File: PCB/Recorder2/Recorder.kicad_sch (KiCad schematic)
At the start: 57 parts, among them J1 Reset, J2 JST-PH-SM4-TB, J3 TC2030-USB-NL-DS, J4 TF_PUSH, J5 USB-C-Socket-H, Q1 CJ2301, SW1 SW_Push_DPDT, U1 ESP32-S3-MINI-1-N4R2, U3 TP4054, U4 ME6211C33M5G-N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

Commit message: Tracked for order
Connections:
- net ADC: now also U1.14 (GPIO10)
- net ADCL: now also U1.15 (GPIO11)
- net BLINK: now also U1.29 (GPIO34); no longer U1.35 (GPIO39)
- net BTN: now also U1.7 (GPIO3); no longer U1.5 (GPIO1)
- net CHARGING: now also U1.5 (GPIO1); no longer U1.15 (GPIO11)
- net LEDMIC: now also U1.13 (GPIO9); no longer U1.12 (GPIO8)
- net at U1.30 (GPIO48): now also R1.1
- net at U1.37 (GPIO41): no longer R1.1
- net VIN: no longer names the net of D3.1 (K), Q1.2 (S), U4.1 (IN), U4.3 (EN)
- no-connect marks 22 -> 20
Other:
- moved on the sheet: R1
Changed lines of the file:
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@@
 	)
 	(junction
-		(at 196.85 133.985)
-		(diameter 0)
-		(color 0 0 0 0)
-	)
-	(junction
 		(at 247.65 22.86)
 		(diameter 0)
@@
 	)
 	(no_connect
-		(at 66.04 88.9)
+		(at 66.04 86.36)
 	)
 	(no_connect
@@
 	)
 	(no_connect
-		(at 66.04 101.6)
+		(at 66.04 81.28)
 	)
 	(no_connect
@@
 	)
 	(no_connect
-		(at 35.56 58.42)
-	)
-	(no_connect
 		(at 66.04 71.12)
 	)
@@
 	)
 	(no_connect
-		(at 35.56 73.66)
-	)
-	(no_connect
 		(at 66.04 93.98)
 	)
 	(no_connect
-		(at 35.56 55.88)
+		(at 35.56 58.42)
 	)
 	(no_connect
@@
 	)
 	(no_connect
-		(at 66.04 68.58)
+		(at 66.04 88.9)
 	)
 	(no_connect
@@
 	)
 	(no_connect
-		(at 35.56 71.12)
+		(at 35.56 68.58)
 	)
 	(wire
@@
 	(wire
 		(pts
+			(xy 73.66 90.805) (xy 70.485 90.805)
+		)
+		(stroke
+			(width 0)
+			(type default)
+		)
+	)
+	(wire
+		(pts
 			(xy 273.05 121.285) (xy 273.05 122.555)
 		)
@@
 	(wire
 		(pts
+			(xy 70.485 90.805) (xy 70.485 101.6)
+		)
+		(stroke
+			(width 0)
+			(type default)
+		)
+	)
+	(wire
+		(pts
 			(xy 137.16 70.485) (xy 137.16 74.295)
 		)
@@
 	(wire
 		(pts
+			(xy 70.485 101.6) (xy 66.04 101.6)
+		)
+		(stroke
+			(width 0)
+			(type default)
+		)
+	)
+	(wire
+		(pts
 			(xy 121.92 62.865) (xy 125.73 62.865)
 		)
@@
 	(wire
 		(pts
-			(xy 196.85 133.985) (xy 196.85 139.7)
-		)
-		(stroke
-			(width 0)
-			(type default)
-		)
-	)
-	(wire
-		(pts
 			(xy 110.49 76.835) (xy 133.35 76.835)
 		)
@@
 	(global_label "BTN"
 		(shape input)
-		(at 35.56 50.8 180)
+		(at 35.56 55.88 180)
 		(fields_autoplaced yes)
 		(effects
@@
 		)
 		(property "Intersheetrefs" "${INTERSHEET_REFS}"
-			(at 29.6609 50.8 0)
+			(at 29.6609 55.88 0)
 			(effects
 				(font
@@
 	(global_label "CHARGING"
 		(shape input)
-		(at 35.56 76.2 180)
-		(fields_autoplaced yes)
-		(effects
-			(font
-				(size 1.27 1.27)
-			)
-			(justify right)
-		)
-		(property "Intersheetrefs" "${INTERSHEET_REFS}"
-			(at 23.7946 76.2 0)
-			(effects
-				(font
-					(size 1.27 1.27)
-				)
-				(justify right)
-				(hide yes)
-			)
-		)
-	)
-	(global_label "VIN"
-		(shape output)
-		(at 196.85 139.7 270)
+		(at 35.56 50.8 180)
 		(fields_autoplaced yes)
 		(effects
@@
 		)
 		(property "Intersheetrefs" "${INTERSHEET_REFS}"
-			(at 196.85 145.0549 90)
+			(at 23.7946 50.8 0)
 			(effects
 				(font
@@
 		)
 	)
+	(global_label "ADC"
+		(shape input)
+		(at 35.56 73.66 180)
+		(effects
+			(font
+				(size 1.27 1.27)
+			)
+			(justify right)
+		)
+		(property "Intersheetrefs" "${INTERSHEET_REFS}"
+			(at 35.56 73.66 0)
+			(effects
+				(font
+					(size 1.27 1.27)
+				)
+				(hide yes)
+			)
+		)
+	)
 	(global_label "VBUS"
 		(shape output)
@@
 	(global_label "VBUS"
 		(shape input)
-		(at 73.66 86.36 0)
+		(at 81.28 90.805 0)
 		(fields_autoplaced yes)
 		(effects
@@
 		)
 		(property "Intersheetrefs" "${INTERSHEET_REFS}"
-			(at 80.8896 86.36 0)
+			(at 88.5096 90.805 0)
 			(effects
 				(font
@@
 	(global_label "LEDMIC"
 		(shape output)
-		(at 35.56 68.58 180)
+		(at 35.56 71.12 180)
 		(fields_autoplaced yes)
 		(effects
@@
 		)
 		(property "Intersheetrefs" "${INTERSHEET_REFS}"
-			(at 26.4557 68.58 0)
+			(at 26.4557 71.12 0)
 			(effects
 				(font
@@
 	(global_label "BLINK"
 		(shape output)
-		(at 66.04 81.28 0)
+		(at 66.04 68.58 0)
 		(fields_autoplaced yes)
 		(effects
@@
 		)
 		(property "Intersheetrefs" "${INTERSHEET_REFS}"
-			(at 73.8744 81.28 0)
+			(at 73.8744 68.58 0)
 			(effects
 				(font
@@
 		)
 	)
+	(global_label "ADCL"
+		(shape bidirectional)
+		(at 35.56 76.2 180)
+		(effects
+			(font
+				(size 1.27 1.27)
+			)
+			(justify right)
+		)
+		(property "Intersheetrefs" "${INTERSHEET_REFS}"
+			(at 35.56 76.2 0)
+			(effects
+				(font
+					(size 1.27 1.27)
+				)
+				(hide yes)
+			)
+		)
+	)
 	(global_label "SDDAT2"
 		(shape bidirectional)
@@
 	(symbol
 		(lib_id "Device:R")
-		(at 69.85 86.36 90)
+		(at 77.47 90.805 90)
 		(unit 1)
 		(exclude_from_sim no)
@@
 		(dnp no)
 		(property "Reference" "R1"
-			(at 69.85 84.455 90)
+			(at 77.47 88.9 90)
 			(effects
 				(font
@@
 		)
 		(property "Value" "10K"
-			(at 69.85 86.36 90)
+			(at 77.47 90.805 90)
 			(effects
 				(font
@@
 		)
 		(property "Footprint" "RevK:R_0201"
-			(at 69.85 88.138 90)
+			(at 77.47 92.583 90)
 			(effects
 				(font
@@
 		)
 		(property "Datasheet" "~"
-			(at 69.85 86.36 0)
+			(at 77.47 90.805 0)
 			(effects
 				(font
@@
 		)
 		(property "Description" "Resistor"
-			(at 69.85 86.36 0)
+			(at 77.47 90.805 0)
 			(effects
 				(font

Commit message: Re render
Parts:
- C10, C11: footprint RevK:C_0402 -> RevK:C_0201
- J2: Rotation Offset (none) -> 180
- R1, R10, R2, R3, R4, R5, R6, R7, R9: MPN (none) -> C106225
- R11: footprint RevK:R_0402 -> RevK:R_0201; MPN (none) -> C106225
- R12, R13: MPN (none) -> C274341
- R14, R15, R16: footprint RevK:R_0402 -> RevK:R_0201; MPN C5139597 -> C717003
- R8: value 10K -> 5K1; footprint RevK:R_0402 -> RevK:R_0201; MPN (none) -> C274341
- U4: Rotation Offset (none) -> 90
- U5: value L -> ICS-43434
- U6: value R -> ICS-43434
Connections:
- net ADC: now also U1.15 (GPIO11); no longer U1.14 (GPIO10)
- net GND: now also R16.2
- removed net ADCL: R16.2, U1.15 (GPIO11)
- no-connect marks 20 -> 21
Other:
- note added: "5k1 is approx 200mA charge"
- note added: "CHRG Normal: on Full: off Reverse: off No battery: Twinkle"
- note added: "L"
- note added: "R"

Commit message: Layout tweaks
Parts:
- U2: value ~ -> TPS22916CNYFPR
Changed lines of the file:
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@@
 			)
 		)
-		(property "Value" "~"
+		(property "Value" "TPS22916CNYFPR"
 			(at 67.818 143.2949 0)
 			(effects

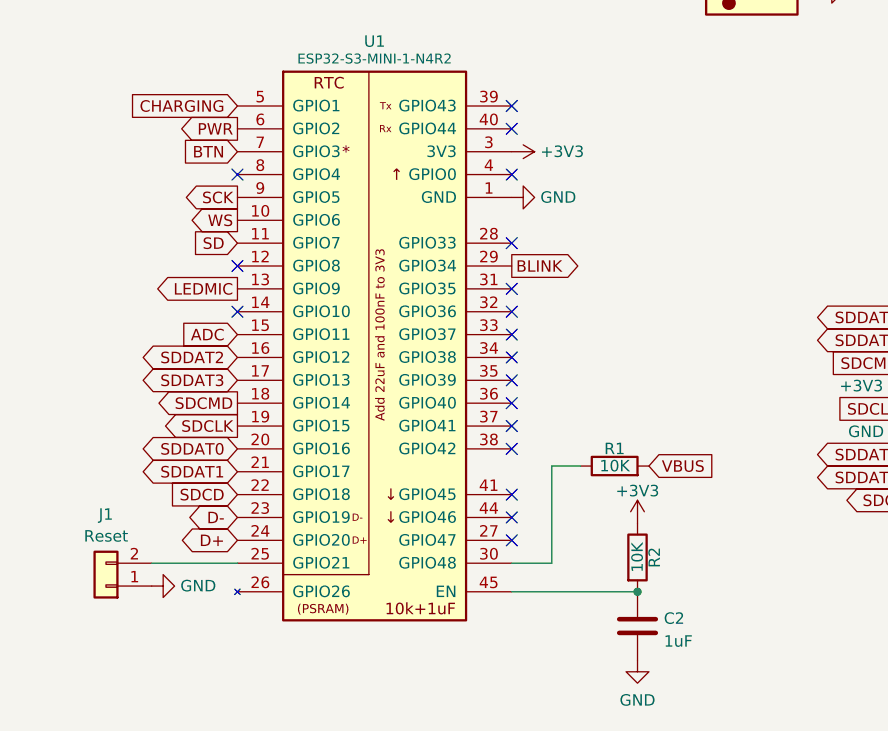
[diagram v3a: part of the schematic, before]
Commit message: Moved GPIOs around a bit
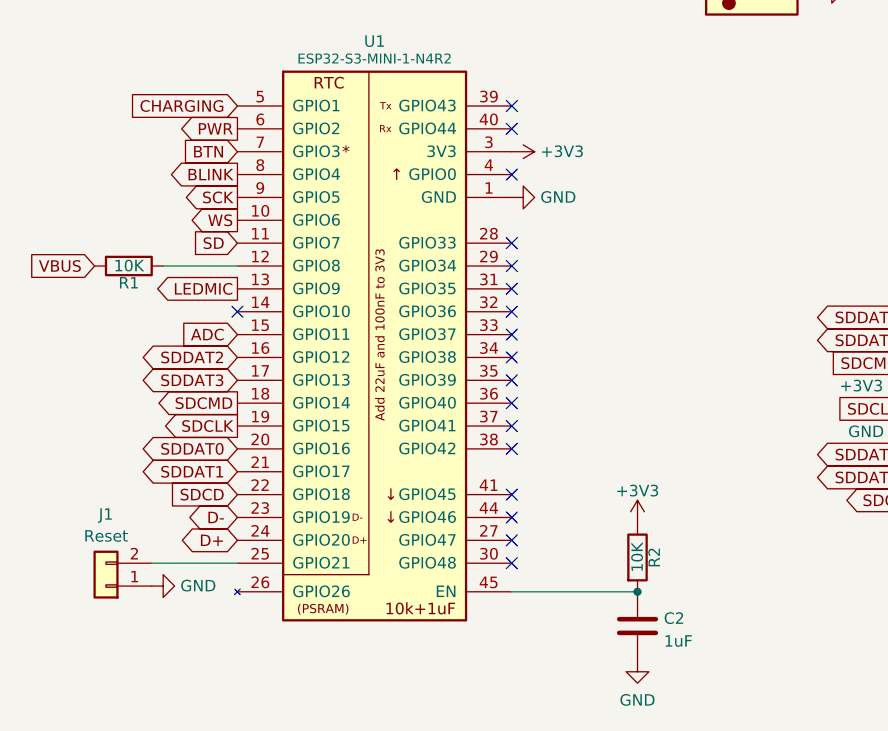
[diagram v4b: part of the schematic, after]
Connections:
- net BLINK: now also U1.8 (GPIO4); no longer U1.29 (GPIO34)
- net at U1.12 (GPIO8): now also R1.1
- net at U1.30 (GPIO48): no longer R1.1
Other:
- moved on the sheet: R1
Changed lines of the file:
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@@
 	)
 	(no_connect
-		(at 35.56 58.42)
+		(at 66.04 68.58)
 	)
 	(no_connect
@@
 	)
 	(no_connect
-		(at 35.56 68.58)
+		(at 66.04 101.6)
 	)
 	(wire
@@
 	(wire
 		(pts
-			(xy 73.66 90.805) (xy 70.485 90.805)
-		)
-		(stroke
-			(width 0)
-			(type default)
-		)
-	)
-	(wire
-		(pts
 			(xy 273.05 121.285) (xy 273.05 122.555)
 		)
@@
 	(wire
 		(pts
-			(xy 70.485 90.805) (xy 70.485 101.6)
-		)
-		(stroke
-			(width 0)
-			(type default)
-		)
-	)
-	(wire
-		(pts
 			(xy 137.16 70.485) (xy 137.16 74.295)
 		)
@@
 	(wire
 		(pts
-			(xy 239.395 52.705) (xy 239.395 57.15)
+			(xy 27.305 68.58) (xy 35.56 68.58)
 		)
 		(stroke
@@
 	(wire
 		(pts
-			(xy 57.785 156.845) (xy 57.785 164.465)
+			(xy 239.395 52.705) (xy 239.395 57.15)
 		)
 		(stroke
@@
 	(wire
 		(pts
-			(xy 133.35 62.865) (xy 137.16 62.865)
+			(xy 57.785 156.845) (xy 57.785 164.465)
 		)
 		(stroke
@@
 	(wire
 		(pts
-			(xy 186.055 133.985) (xy 180.975 133.985)
+			(xy 133.35 62.865) (xy 137.16 62.865)
 		)
 		(stroke
@@
 	(wire
 		(pts
-			(xy 212.09 126.365) (xy 215.265 126.365)
+			(xy 186.055 133.985) (xy 180.975 133.985)
 		)
 		(stroke
@@
 	(wire
 		(pts
-			(xy 37.465 175.26) (xy 57.785 175.26)
+			(xy 212.09 126.365) (xy 215.265 126.365)
 		)
 		(stroke
@@
 	(wire
 		(pts
-			(xy 114.3 62.865) (xy 111.76 62.865)
+			(xy 37.465 175.26) (xy 57.785 175.26)
 		)
 		(stroke
@@
 	(wire
 		(pts
-			(xy 70.485 101.6) (xy 66.04 101.6)
+			(xy 114.3 62.865) (xy 111.76 62.865)
 		)
 		(stroke
@@
 	(global_label "VBUS"
 		(shape input)
-		(at 81.28 90.805 0)
+		(at 19.685 68.58 180)
 		(fields_autoplaced yes)
 		(effects
@@
 				(size 1.27 1.27)
 			)
-			(justify left)
+			(justify right)
 		)
 		(property "Intersheetrefs" "${INTERSHEET_REFS}"
-			(at 88.5096 90.805 0)
+			(at 12.4554 68.58 0)
 			(effects
 				(font
 					(size 1.27 1.27)
 				)
-				(justify left)
+				(justify right)
 				(hide yes)
 			)
@@
 	(global_label "BLINK"
 		(shape output)
-		(at 66.04 68.58 0)
+		(at 35.56 58.42 180)
 		(fields_autoplaced yes)
 		(effects
@@
 				(size 1.27 1.27)
 			)
-			(justify left)
+			(justify right)
 		)
 		(property "Intersheetrefs" "${INTERSHEET_REFS}"
-			(at 73.8744 68.58 0)
+			(at 27.7256 58.42 0)
 			(effects
 				(font
 					(size 1.27 1.27)
 				)
-				(justify left)
+				(justify right)
 				(hide yes)
 			)
@@
 	(symbol
 		(lib_id "Device:R")
-		(at 77.47 90.805 90)
+		(at 23.495 68.58 270)
 		(unit 1)
 		(exclude_from_sim no)
@@
 		(dnp no)
 		(property "Reference" "R1"
-			(at 77.47 88.9 90)
+			(at 23.495 70.485 90)
 			(effects
 				(font
@@
 		)
 		(property "Value" "10K"
-			(at 77.47 90.805 90)
+			(at 23.495 68.58 90)
 			(effects
 				(font
@@
 		)
 		(property "Footprint" "RevK:R_0201"
-			(at 77.47 92.583 90)
+			(at 23.495 66.802 90)
 			(effects
 				(font
@@
 		)
 		(property "Datasheet" "~"
-			(at 77.47 90.805 0)
+			(at 23.495 68.58 0)
 			(effects
 				(font
@@
 		)
 		(property "Description" "Resistor"
-			(at 77.47 90.805 0)
+			(at 23.495 68.58 0)
 			(effects
 				(font
@@
 		)
 		(property "MPN" "C106225"
-			(at 77.47 90.805 90)
+			(at 23.495 68.58 90)
 			(effects
 				(font

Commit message: Tidy
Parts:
- removed J2: JST-PH-SM4-TB, RevK:JST_PH_S2B-PH-SM4-TB_1x02-1MP_P2.00mm_Horizontal, symbol Connector_Generic:Conn_01x04
- added J6: Battery, RevK:1.25T-2PWT (Molex 532610271), symbol Connector_Generic:Conn_01x02
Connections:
- net GND: now also J6.2 (Pin_2)
- net VBAT: now also J6.1 (Pin_1)
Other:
- moved on the sheet: BT1

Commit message: Twqeak
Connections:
- net GND: no longer SW1.1 (A)
- no-connect marks 21 -> 23
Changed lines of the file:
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@@
 	)
 	(no_connect
+		(at 34.925 155.575)
+	)
+	(no_connect
 		(at 66.04 53.34)
 	)
@@
 	)
 	(no_connect
+		(at 81.28 190.5)
+	)
+	(no_connect
 		(at 266.7 26.67)
 	)
@@
 					(unit 1)
 				)
-			)
-		)
-	)
-	(symbol
-		(lib_id "power:GND")
-		(at 34.925 155.575 180)
-		(unit 1)
-		(exclude_from_sim no)
-		(in_bom yes)
-		(on_board yes)
-		(dnp no)
-		(property "Reference" "#PWR02"
-			(at 34.925 149.225 0)
-			(effects
-				(font
-					(size 1.27 1.27)
-				)
-				(hide yes)
-			)
-		)
-		(property "Value" "GND"
-			(at 34.925 150.495 90)
-			(effects
-				(font
-					(size 1.27 1.27)
-				)
-			)
-		)
-		(property "Footprint" ""
-			(at 34.925 155.575 0)
-			(effects
-				(font
-					(size 1.27 1.27)
-				)
-				(hide yes)
-			)
-		)
-		(property "Datasheet" ""
-			(at 34.925 155.575 0)
-			(effects
-				(font
-					(size 1.27 1.27)
-				)
-				(hide yes)
-			)
-		)
-		(property "Description" "Power symbol creates a global label with name \"GND\" , ground"
-			(at 34.925 155.575 0)
-			(effects
-				(font
-					(size 1.27 1.27)
-				)
-				(hide yes)
-			)
-		)
-		(pin "1"
-		)
-		(instances
-			(project "Recorder"
-				(path "/46c350bb-7de4-4e81-aafd-4af55e37aab0"
-					(reference "#PWR02")
-					(unit 1)
-				)

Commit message: beep bug
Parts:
- added TP1, TP2: TestPoint, RevK:PAD-2mm, symbol Connector:TestPoint
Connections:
- net D+: now also TP2.1
- net D-: now also TP1.1
- net VBAT renamed VBATCHG
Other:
- moved on the sheet: BT1, C1, C3, D2, J6
